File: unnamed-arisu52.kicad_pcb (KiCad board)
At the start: 2 copper layers, 376.6 x 95.8 mm, 129 parts, among them J1 Conn_01x04_Female, SW1 SW_Push, U1 ATmega32U4-M, Y1 Crystal_GND24_Small

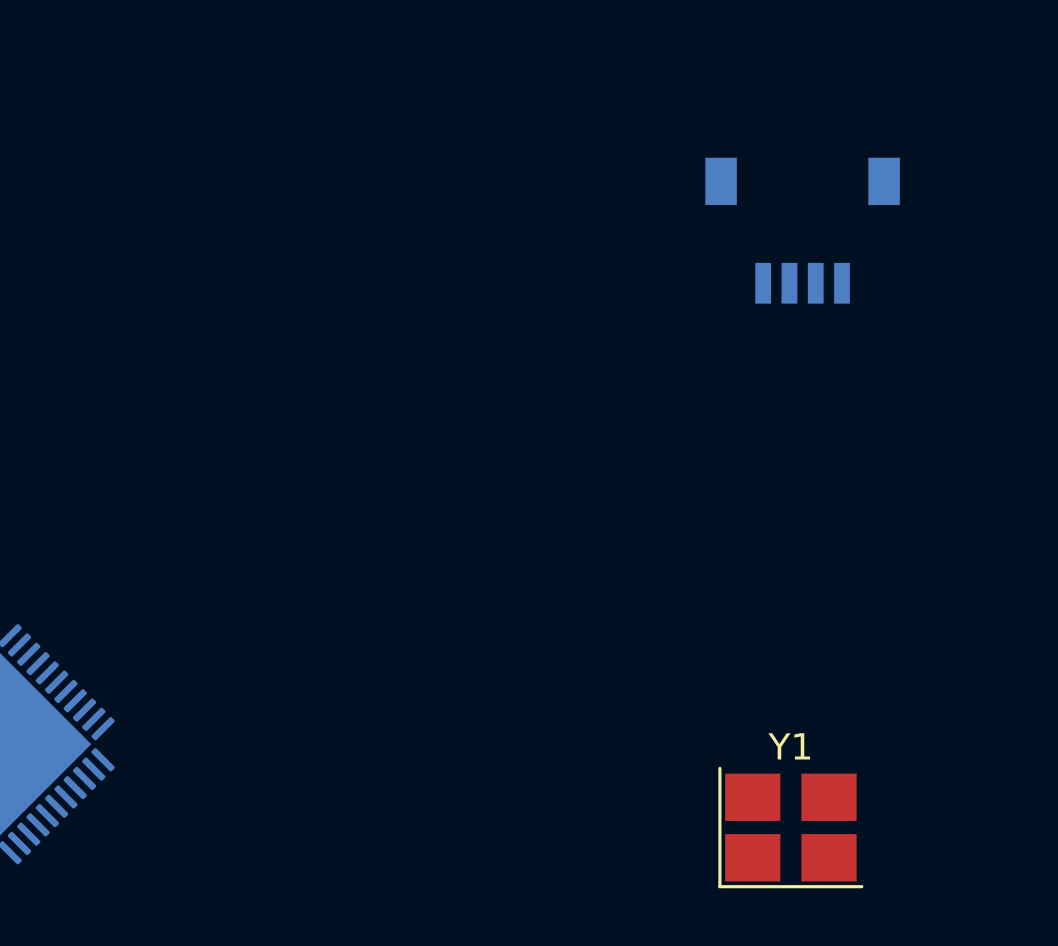
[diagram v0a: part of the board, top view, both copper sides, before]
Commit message: Added README and included reference for pcb layout
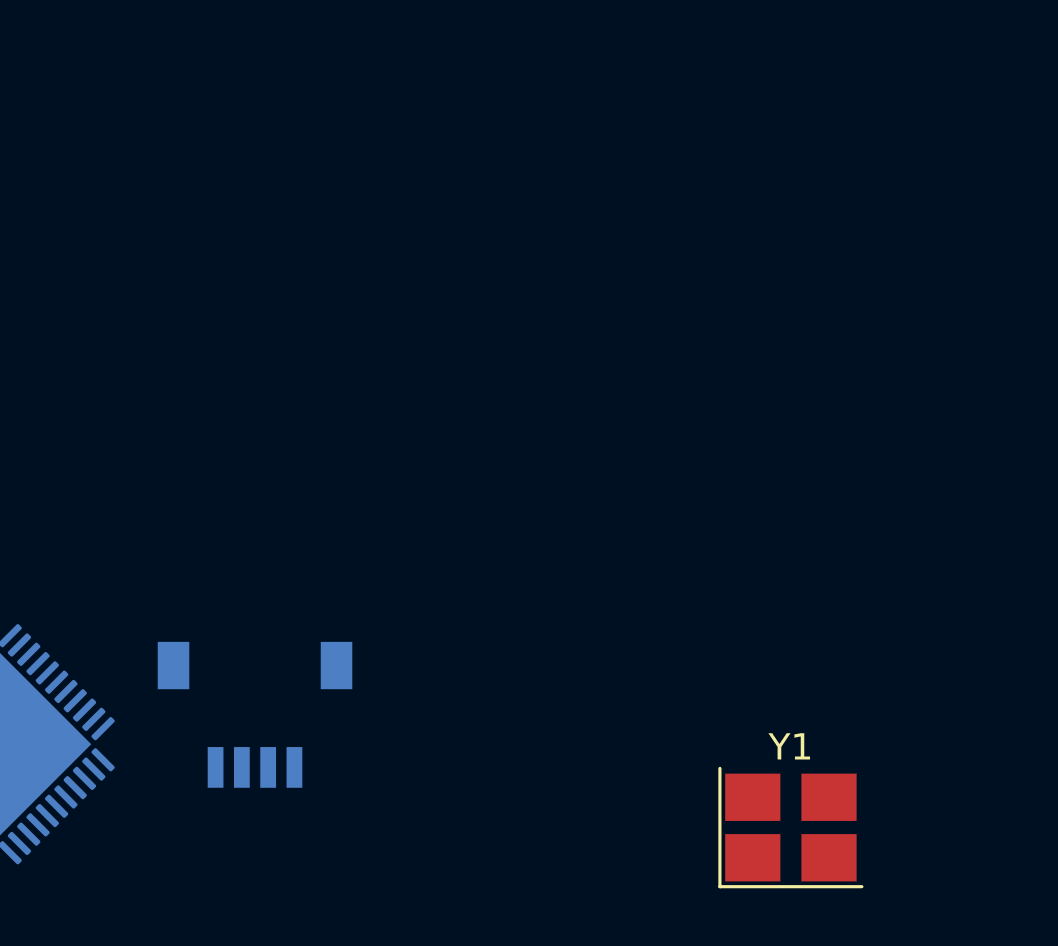
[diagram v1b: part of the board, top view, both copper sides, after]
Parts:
- moved J1 27.8 mm to (189.9, 72.4)
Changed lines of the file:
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@@
   )
   (footprint "acheron_Connectors:SM04B-SRSS-TB(LF)(SN)" (layer "B.Cu")
-    (at 210.693 53.955)
+    (at 189.865 72.37)
     (property "Sheetfile" "unnamed-arisu52.kicad_sch")
     (property "Sheetname" "")

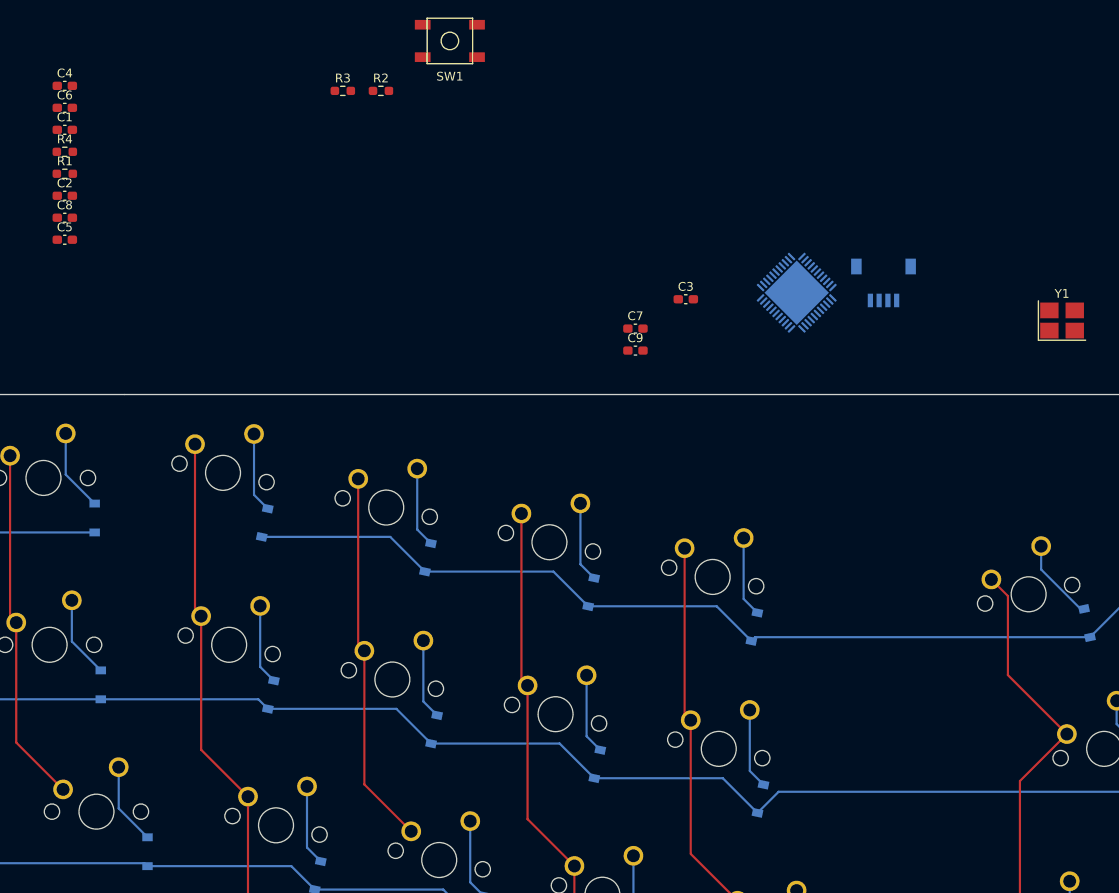
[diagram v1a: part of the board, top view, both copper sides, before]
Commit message: started laying out electronics
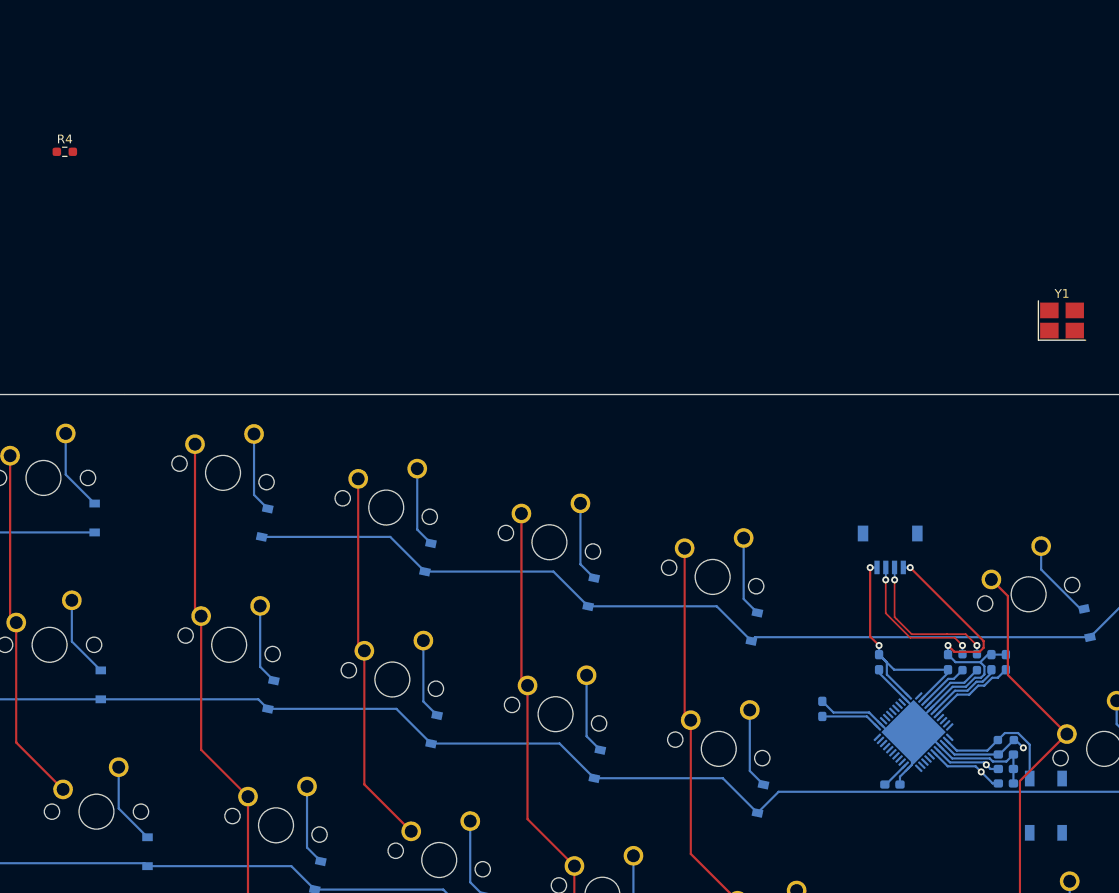
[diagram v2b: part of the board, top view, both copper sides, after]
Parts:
- C1, C2, C3, C4, C5, C6, C7, C8, C9, R1, R2, R3, SW1: moved to B.Cu
- MX50: footprint MX_Only:MXOnly-2U-ReversedStabilizers-NoLED -> MX_Only:MXOnly-2.25U-ReversedStabilizers-NoLED
- moved C1 130.8 mm to (203.8, 128.3), turned to 180 degrees
- moved C2 125.8 mm to (203.8, 126.6), turned to 180 degrees
- moved R1 125.4 mm to (203.8, 123.3), turned to 180 degrees
- moved C6 124.7 mm to (203.8, 114.4), turned to 90 degrees
- moved C5 122.5 mm to (203.8, 125.0)
- moved C4 112.0 mm to (182.9, 119.8), turned to 90 degrees
- moved SW1 110.7 mm to (208.4, 130.8), turned to -90 degrees
- moved C8 105.9 mm to (189.4, 114.4), turned to -90 degrees
- moved R3 96.2 mm to (198.9, 114.4), turned to -90 degrees
- moved R2 94.3 mm to (200.5, 114.4), turned to -90 degrees
- moved C7 59.8 mm to (190.9, 128.4)
- moved C3 54.2 mm to (202.2, 114.4), turned to 90 degrees
- moved U1 51.9 mm to (193.3, 122.4), turned to -135 degrees
- moved C9 50.4 mm to (197.2, 114.4), turned to 90 degrees
- moved J1 30.5 mm to (190.6, 102.8)
- renumbered Dr to D21
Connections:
- C2 pad 2: GND -> Net-(C2-Pad2)
- J1 pad 5: GND -> (no net)
- J1 pad 6: GND -> (no net)
- U1 pad 16: GND -> Net-(C2-Pad2)
- Y1 pad 3: GND -> Net-(C2-Pad2)
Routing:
- net GND: track 0.00 -> 83.5 mm, vias 0 -> 2
- net +5V: track 0.00 -> 61.1 mm, vias 0 -> 3
- net /D+: track 0.00 -> 17.4 mm, vias 0 -> 2
- net /D-: track 0.00 -> 16.5 mm, vias 0 -> 2
- net Net-(R1-Pad2): track 0.00 -> 15.2 mm
- net Net-(C1-Pad2): track 0.00 -> 8.77 mm, vias 0 -> 1
- net Net-(C3-Pad1): track 0.00 -> 8.72 mm
- net Net-(C2-Pad2): track 0.00 -> 7.88 mm, vias 0 -> 1
- net Net-(R2-Pad2): track 0.00 -> 7.25 mm
- net Net-(R3-Pad2): track 0.00 -> 5.80 mm

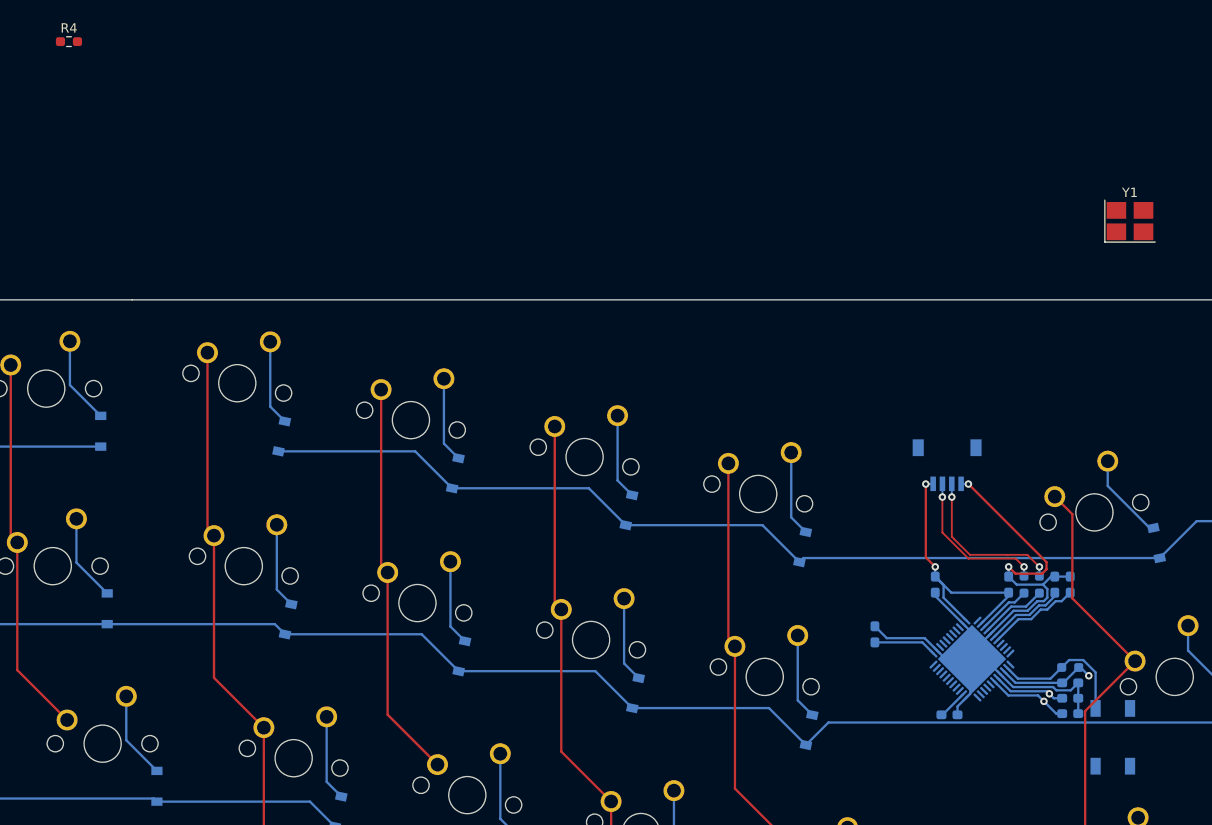
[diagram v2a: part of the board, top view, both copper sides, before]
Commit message: finished wiring electonics, just need to wire matrix
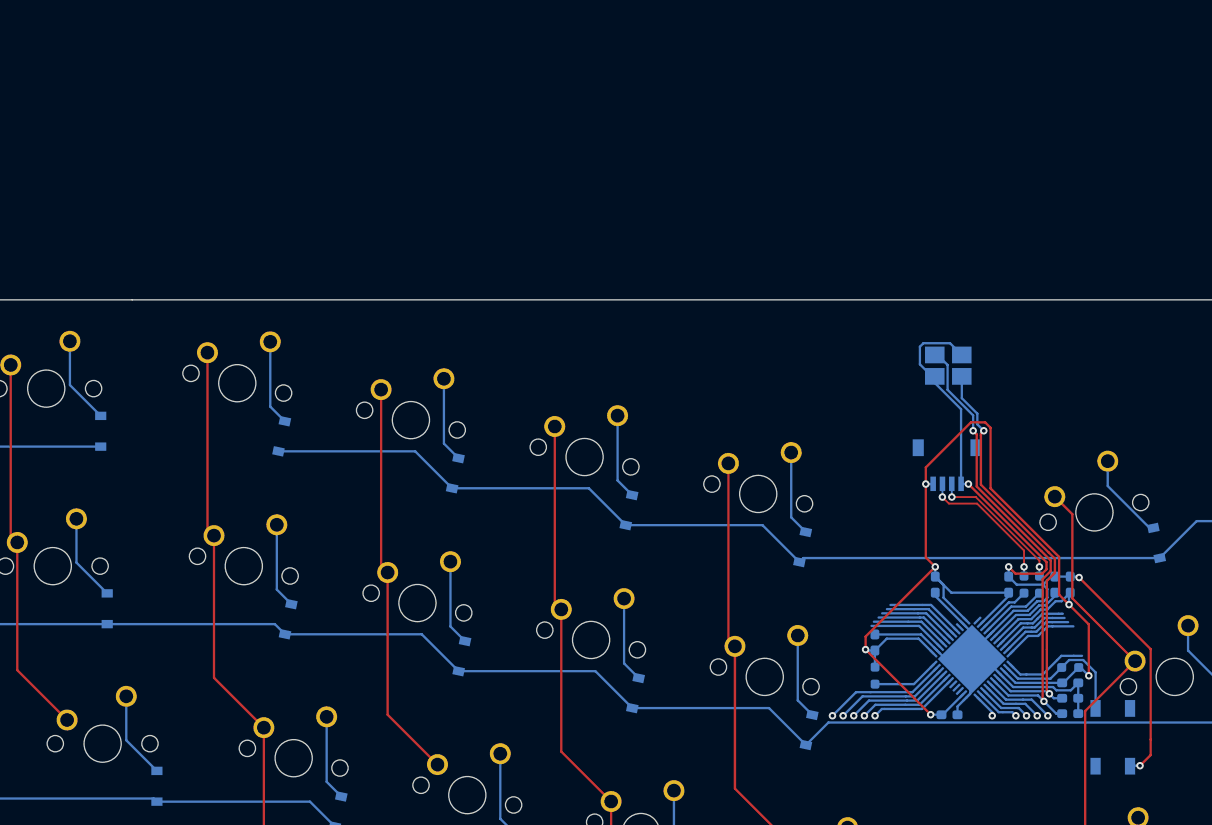
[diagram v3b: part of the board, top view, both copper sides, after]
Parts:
- R4, Y1: moved to B.Cu
- moved R4 110.1 mm to (182.9, 124.2), turned to -90 degrees
- moved Y1 24.9 mm to (190.8, 90.9)
- moved C4 0.87 mm to (182.9, 120.7)
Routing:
- net +5V: track 61.1 -> 130.9 mm, vias 3 -> 6
- net GND: track 83.5 -> 131.0 mm, vias 2 -> 4
- net Net-(C1-Pad2): track 8.77 -> 51.7 mm, vias 1 -> 2
- net Net-(C2-Pad2): track 7.88 -> 46.8 mm, vias 1 -> 2
- net unconnected-(U1-Pad32): track 0.00 -> 13.3 mm, vias 0 -> 1
- net unconnected-(U1-Pad31): track 0.00 -> 12.4 mm, vias 0 -> 1
- net unconnected-(U1-Pad30): track 0.00 -> 11.5 mm, vias 0 -> 1
- net unconnected-(U1-Pad29): track 0.00 -> 10.5 mm, vias 0 -> 1
- net unconnected-(U1-Pad28): track 0.00 -> 9.58 mm, vias 0 -> 1
- net unconnected-(U1-Pad12): track 0.00 -> 8.95 mm
- net unconnected-(U1-Pad37): track 0.00 -> 8.43 mm
- net unconnected-(U1-Pad39): track 0.00 -> 8.33 mm
- net unconnected-(U1-Pad38): track 0.00 -> 8.32 mm
- net unconnected-(U1-Pad36): track 0.00 -> 8.29 mm
- net unconnected-(U1-Pad41): track 0.00 -> 8.23 mm
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
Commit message: routed pins to matrix and resolved some drc issues
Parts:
- moved C7 1.25 mm to (191.8, 129.3), turned to -90 degrees
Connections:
- U1 pad 10: unconnected-(U1-Pad10) -> /ROW-2
- U1 pad 11: unconnected-(U1-Pad11) -> /ROW-3
- U1 pad 18: unconnected-(U1-Pad18) -> /COL-7
- U1 pad 19: unconnected-(U1-Pad19) -> /COL-8
- U1 pad 20: unconnected-(U1-Pad20) -> /COL-9
- U1 pad 21: unconnected-(U1-Pad21) -> /COL-10
- U1 pad 22: unconnected-(U1-Pad22) -> /COL-11
- U1 pad 25: unconnected-(U1-Pad25) -> /COL-13
- U1 pad 26: unconnected-(U1-Pad26) -> /COL-12
- U1 pad 27: unconnected-(U1-Pad27) -> /COL-14
- U1 pad 28: unconnected-(U1-Pad28) -> /COL-15
- U1 pad 29: unconnected-(U1-Pad29) -> /COL-0
- U1 pad 30: unconnected-(U1-Pad30) -> /COL-1
- U1 pad 31: unconnected-(U1-Pad31) -> /COL-2
- U1 pad 32: unconnected-(U1-Pad32) -> /COL-3
- U1 pad 36: unconnected-(U1-Pad36) -> /COL-4
- U1 pad 37: unconnected-(U1-Pad37) -> /COL-5
- U1 pad 38: unconnected-(U1-Pad38) -> /COL-6
- U1 pad 8: unconnected-(U1-Pad8) -> /ROW-0
- U1 pad 9: unconnected-(U1-Pad9) -> /ROW-1
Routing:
- net /ROW-3: track 333.7 -> 596.8 mm, vias 0 -> 2
- net /COL-0: track 42.0 -> 280.3 mm, vias 0 -> 1
- net /ROW-2: track 374.1 -> 612.1 mm, vias 0 -> 2
- net /COL-15: track 67.8 -> 294.9 mm, vias 0 -> 1
- net /ROW-1: track 361.8 -> 585.1 mm
- net /COL-14: track 69.4 -> 275.1 mm, vias 0 -> 1
- net /COL-1: track 65.0 -> 262.6 mm, vias 0 -> 1
- net /COL-13: track 82.6 -> 265.0 mm, vias 0 -> 1
- net /COL-2: track 40.6 -> 213.4 mm, vias 0 -> 1
- net /COL-12: track 44.1 -> 200.7 mm, vias 0 -> 1
- net /COL-11: track 44.9 -> 188.9 mm, vias 0 -> 1
- net /COL-4: track 42.7 -> 186.4 mm, vias 0 -> 1
- net /COL-3: track 64.7 -> 207.6 mm, vias 0 -> 1
- net /COL-5: track 63.5 -> 177.7 mm, vias 0 -> 1
- net /COL-10: track 66.0 -> 177.3 mm, vias 0 -> 1
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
